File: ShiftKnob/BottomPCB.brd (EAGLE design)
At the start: 37.8 x 40.2 mm, 39 parts, among them IC2 7805DT, J1 AVR_SPI_PRG_6PTH, Q1 16MHz, Q2 MOSFET-NCHANNELSMD, Q3 MOSFET-PCHANNELSMD, Q4 MOSFET-NCHANNELSMD, Q5 MOSFET-NCHANNELSMD, Q6 MOSFET-NCHANNELSMD, U1 ATMEGA328

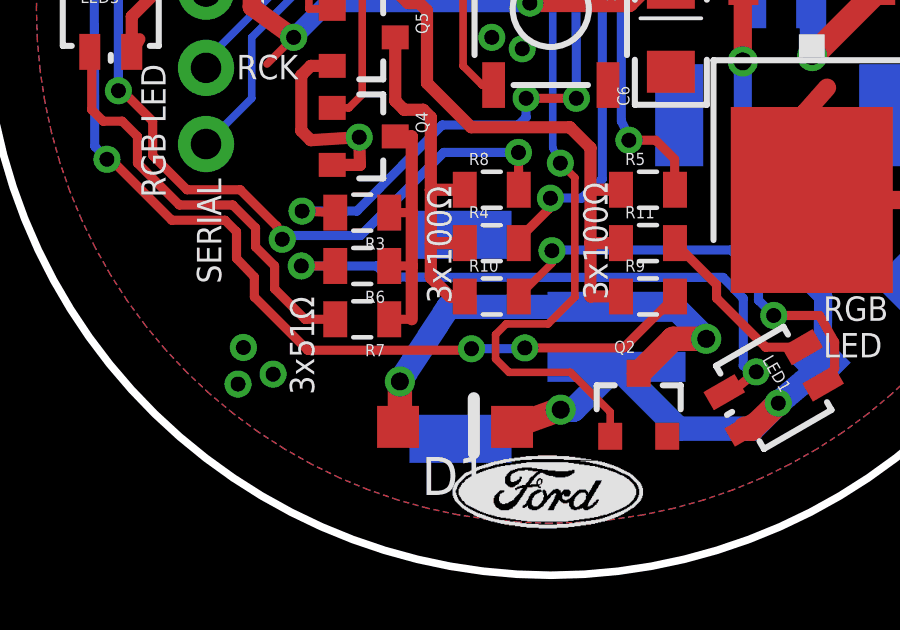
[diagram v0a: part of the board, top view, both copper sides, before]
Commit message: change red LED resistance from 50ohm to 100ohm.
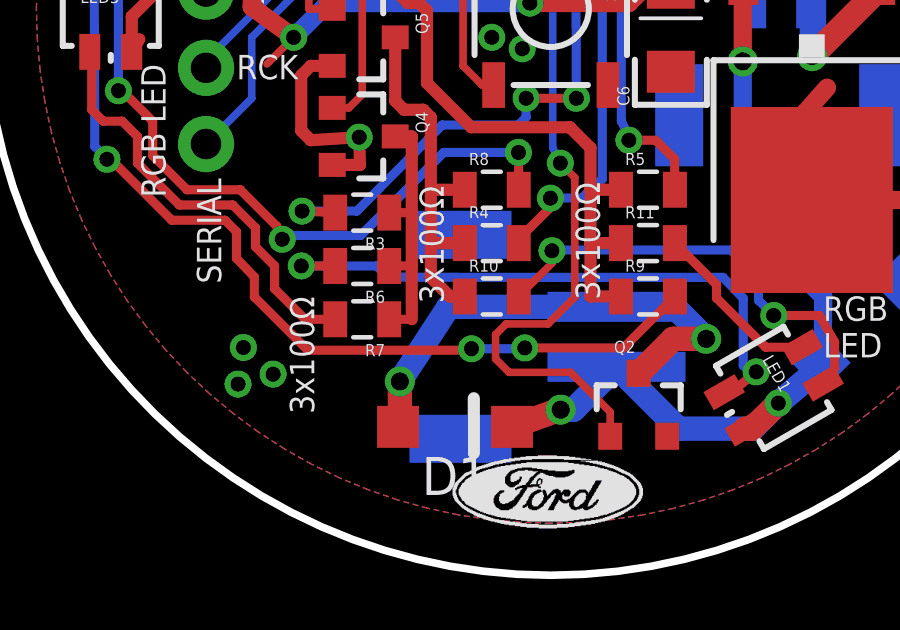
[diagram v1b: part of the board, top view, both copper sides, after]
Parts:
- R3, R6, R7: value 50 -> 100
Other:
- board text removed: "3x51Ω"
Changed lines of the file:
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@@
 <rectangle x1="15.7759" y1="22.3545" x2="16.4109" y2="22.3799" layer="22" rot="R90"/>
 <text x="20.386" y="24.577" size="0.8128" layer="21">BUT</text>
-<text x="12.893" y="12.004" size="0.8128" layer="21" rot="R270">3x51Ω</text>
-<text x="17.465" y="15.687" size="0.8128" layer="21" rot="R270">3x100Ω</text>
-<text x="22.672" y="15.814" size="0.8128" layer="21" rot="R270">3x100Ω</text>
+<text x="12.893" y="12.004" size="0.8128" layer="21" rot="R270">3x100Ω</text>
+<text x="17.211" y="15.687" size="0.8128" layer="21" rot="R270">3x100Ω</text>
+<text x="22.418" y="15.814" size="0.8128" layer="21" rot="R270">3x100Ω</text>
 <rectangle x1="21.1861" y1="4.2697" x2="21.7957" y2="4.2951" layer="21"/>
 <rectangle x1="20.7797" y1="4.2951" x2="22.1767" y2="4.3205" layer="21"/>
@@
 <element name="LED4" library="SparkFun" package="LED-0603" value="Red" x="29.403" y="26.863"/>
 <element name="R4" library="SparkFun-Resistors" package="0805" value="100" x="19.624" y="13.782"/>
-<element name="R3" library="SparkFun-Resistors" package="0805" value="50" x="15.306" y="14.798" rot="R180"/>
+<element name="R3" library="SparkFun-Resistors" package="0805" value="100" x="15.306" y="14.798" rot="R180"/>
 <element name="R5" library="SparkFun-Resistors" package="0805" value="100" x="24.831" y="15.56"/>
-<element name="R7" library="SparkFun-Resistors" package="0805" value="50" x="15.306" y="11.242" rot="R180"/>
+<element name="R7" library="SparkFun-Resistors" package="0805" value="100" x="15.306" y="11.242" rot="R180"/>
 <element name="R8" library="SparkFun-Resistors" package="0805" value="100" x="19.624" y="15.56"/>
 <element name="R9" library="SparkFun-Resistors" package="0805" value="100" x="24.831" y="12.004"/>
@@
 <element name="D1" library="diode" package="SOD123" value="MBR0520LT" x="18.3998" y="7.6556" rot="R180"/>
 <element name="LED1" library="SparkFun" package="LED-TRICOLOR-SMD" value="LED-TRICOLOR" x="29.022" y="8.956" rot="R300"/>
-<element name="R6" library="SparkFun-Resistors" package="0805" value="50" x="15.306" y="13.02" rot="R180"/>
+<element name="R6" library="SparkFun-Resistors" package="0805" value="100" x="15.306" y="13.02" rot="R180"/>
 <element name="R10" library="SparkFun-Resistors" package="0805" value="100" x="19.624" y="12.004"/>
 <element name="R11" library="SparkFun-Resistors" package="0805" value="100" x="24.831" y="13.782"/>

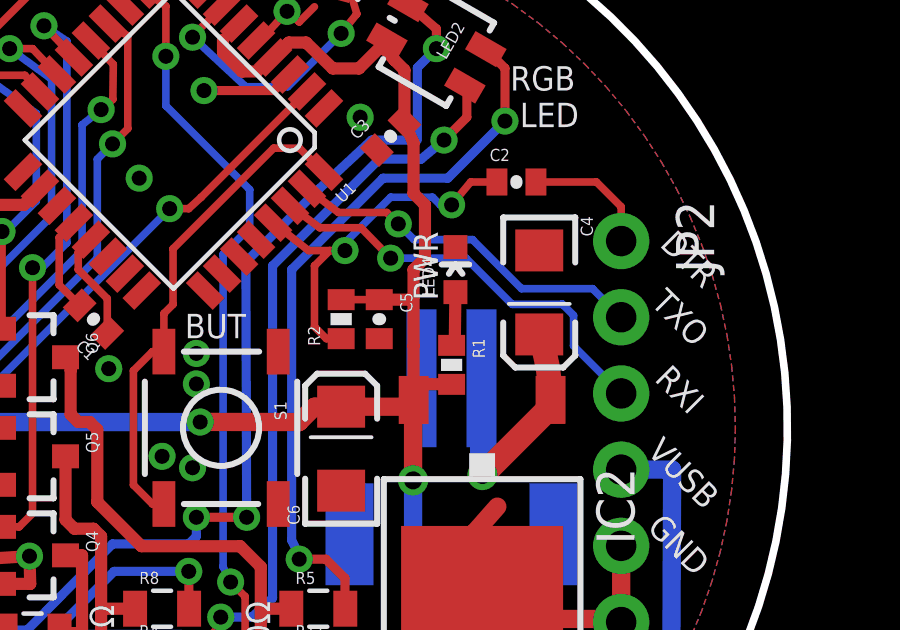
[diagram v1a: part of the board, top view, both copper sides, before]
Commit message: remove power LED and resistor. not needed as RGB leds turn on when 5V is applied during startup.
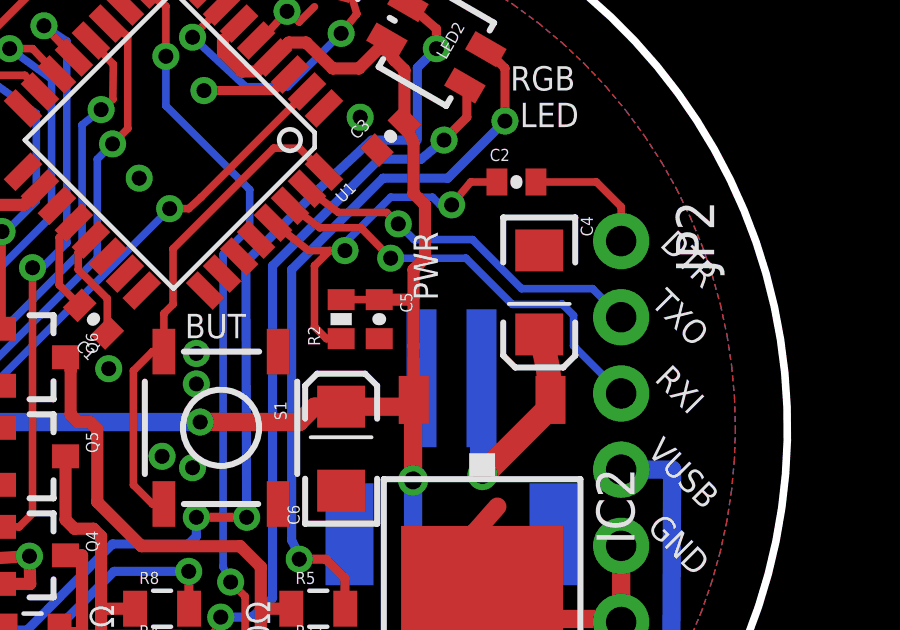
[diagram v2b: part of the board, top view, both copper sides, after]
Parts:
- removed LED4: Red, SparkFun:LED-0603
- removed R1: 10K, SparkFun:0402-RES
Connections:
- removed net N$3: LED4.A, R1.1
- net GND: no longer LED4.C
- net VCC: no longer R1.2
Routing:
- net N$3: track 1.91 -> 0.00 mm
- net VCC: track 94.5 -> 93.2 mm
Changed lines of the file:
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@@
 <element name="C5" library="SparkFun" package="0402-CAP" value="0.1uF" x="26.863" y="25.212" rot="R270"/>
 <element name="C6" library="SparkFun" package="EIA3216" value="10uF" x="25.593" y="20.894" rot="R90"/>
-<element name="R1" library="SparkFun" package="0402-RES" value="10K" x="29.276" y="23.688" rot="R270"/>
-<element name="LED4" library="SparkFun" package="LED-0603" value="Red" x="29.403" y="26.863"/>
 <element name="R4" library="SparkFun-Resistors" package="0805" value="100" x="19.624" y="13.782"/>
 <element name="R3" library="SparkFun-Resistors" package="0805" value="100" x="15.306" y="14.798" rot="R180"/>
@@
 <contactref element="C6" pad="C"/>
 <contactref element="C5" pad="2"/>
-<contactref element="LED4" pad="C"/>
 <contactref element="Q4" pad="2"/>
 <contactref element="Q5" pad="2"/>
@@
 <contactref element="C6" pad="A"/>
 <contactref element="C5" pad="1"/>
-<contactref element="R1" pad="2"/>
 <contactref element="LED2" pad="A"/>
 <contactref element="LED3" pad="A"/>
@@
 <wire x1="27.371" y1="33.848" x2="27.70361875" y2="33.51538125" width="0.4064" layer="1"/>
 <wire x1="27.70361875" y1="33.51538125" x2="27.70361875" y2="31.76761875" width="0.4064" layer="1"/>
-<wire x1="28.021" y1="23.053" x2="29.276" y2="23.038" width="0.4064" layer="1"/>
 <wire x1="25.593" y1="25.862" x2="26.863" y2="25.862" width="0.254" layer="1"/>
 <wire x1="26.863" y1="25.862" x2="27.894" y2="25.862" width="0.4064" layer="1"/>
@@
 <wire x1="26.863" y1="30.546" x2="23.307" y2="26.99" width="0.3048" layer="16"/>
 </signal>
-<signal name="N$3">
-<contactref element="R1" pad="1"/>
-<contactref element="LED4" pad="A"/>
-<wire x1="29.276" y1="24.338" x2="29.3792" y2="24.3126" width="0.4064" layer="1"/>
-<wire x1="29.3792" y1="24.3126" x2="29.403" y2="26.113" width="0.4064" layer="1"/>
-</signal>
 <signal name="N$4">

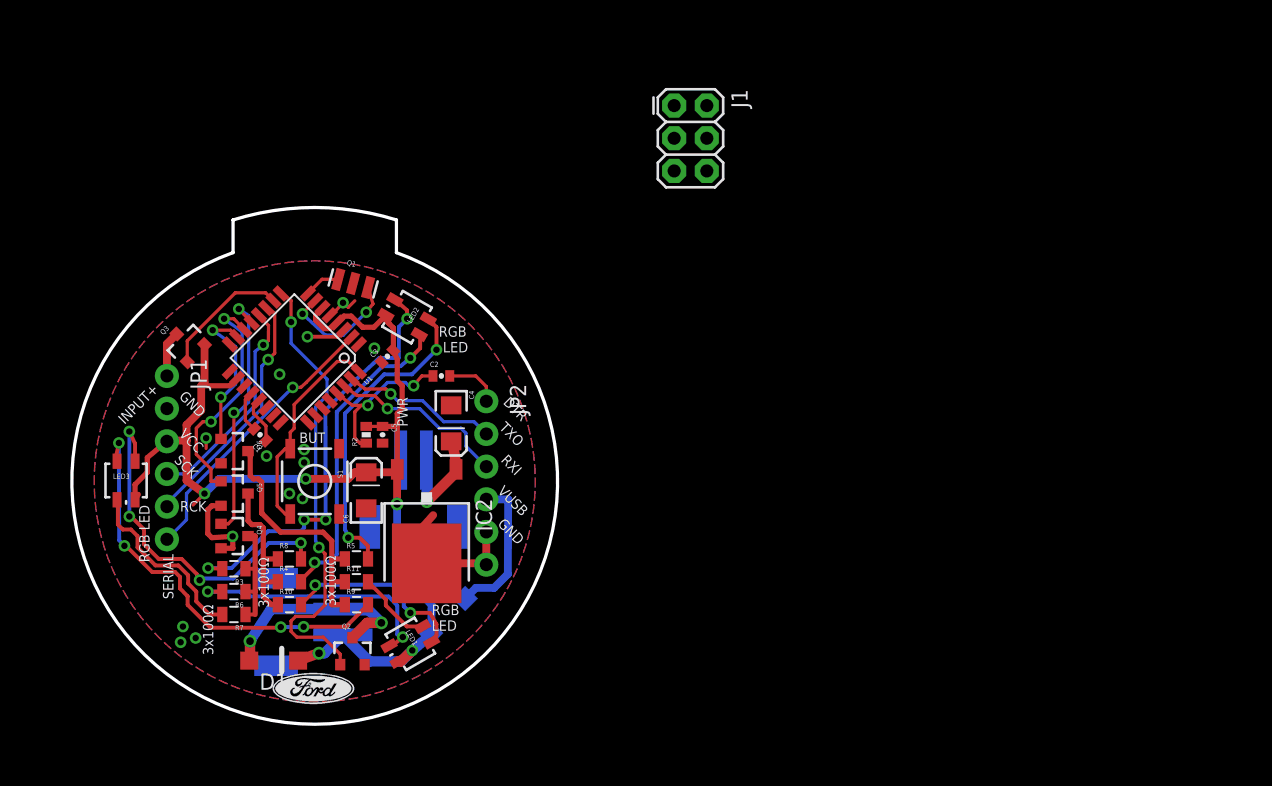
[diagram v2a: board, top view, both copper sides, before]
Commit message: finish the schematic for the FTDI chip. Need to rework the board layout still.
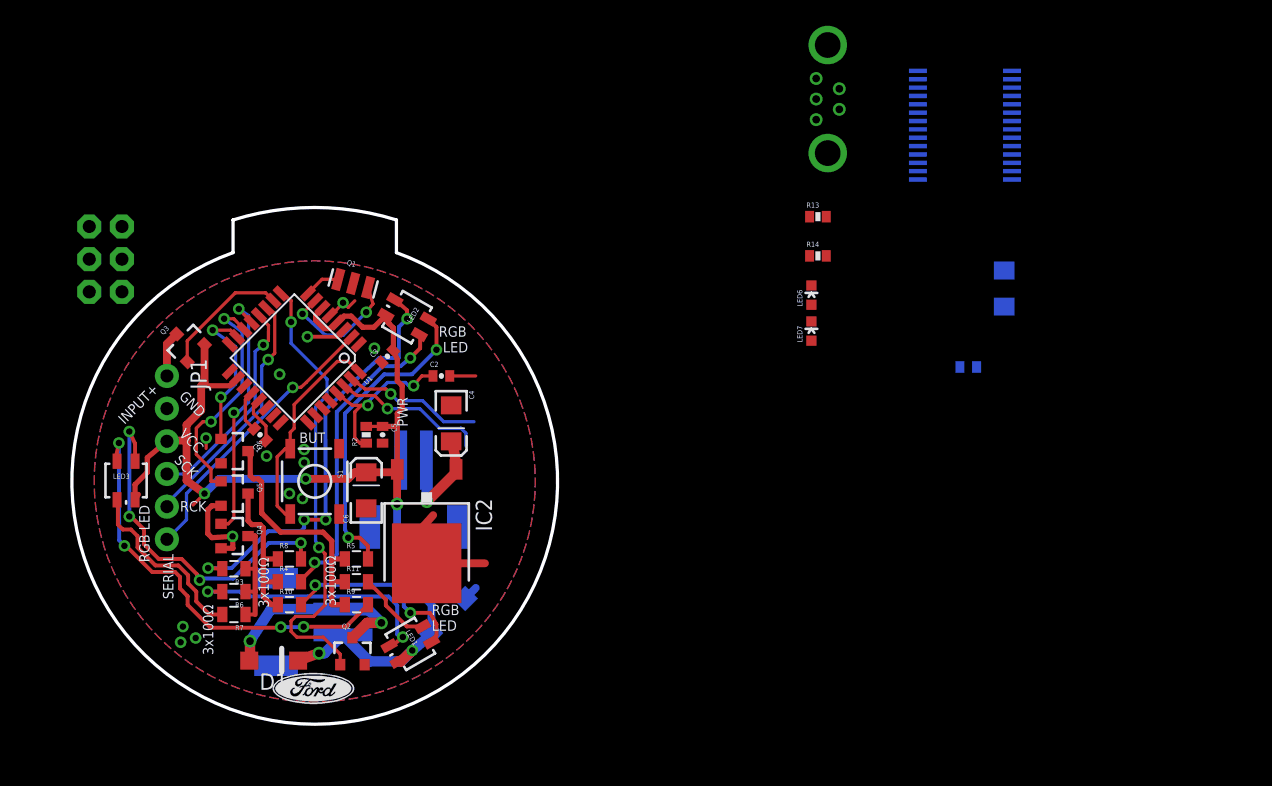
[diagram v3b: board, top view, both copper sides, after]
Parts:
- removed JP2: FTDI Basic, SparkFun-Connectors:1X06
- added C10: 10uF, SparkFun:EIA3216
- added C9: 0.1uF, SparkFun:0402-CAP
- added LED6: Red, SparkFun:LED-0603
- added LED7: Green, SparkFun:LED-0603
- added R13, R14: 1K, SparkFun:0402-RES
- added U$6: USB-MINI-B_VERTICAL, FORD_frames:USB-MINI-B_VERTICAL
- added U3: FT232RL-BASICSSOP, SparkFun-DigitalIC:SSOP28DB
- moved J1 43.9 mm to (6.60, 41.4), flipped to the bottom
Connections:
- new net 5V: R13.2, R14.2
- new net N$21: U$6.D+, U3.15
- new net N$22: U$6.D-, U3.16
- new net N$23: LED6.A, R13.1
- new net N$24: LED7.A, R14.1
- new net RXLED1: LED7.C, U3.22
- new net TXLED1: LED6.C, U3.23
- net DTR: now also U3.2; no longer JP2.1
- net GND: now also C10.C, C9.2, U$6.GND, U3.18, U3.21, U3.25, U3.26, U3.7; no longer JP2.5, JP2.6
- net RXI: now also U3.5; no longer JP2.3
- net TXO: now also U3.1; no longer JP2.2
- net VUSB: now also C10.A, C9.1, U$6.VUSB, U3.20, U3.4; no longer JP2.4
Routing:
- net VUSB: track 11.6 -> 1.17 mm
- net GND: track 28.5 -> 25.8 mm
- net DTR: track 4.33 -> 2.02 mm
- net RXI: track 14.2 -> 11.9 mm
- net TXO: track 12.2 -> 10.8 mm
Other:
- board text removed: "DTR"
- board text removed: "RXI"
- board text removed: "TXO"
- board text removed: "VUSB"

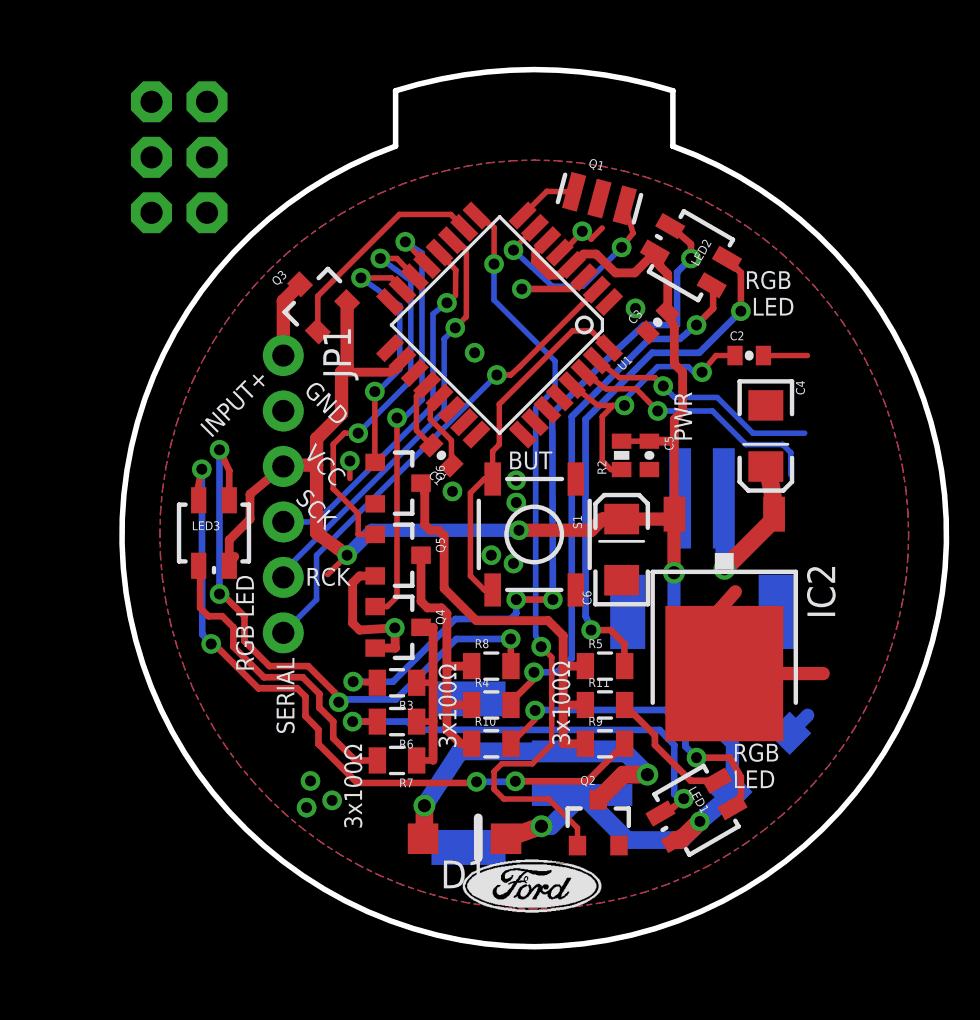
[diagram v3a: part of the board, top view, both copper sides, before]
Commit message: switch out RGB LEDs for Right-Angle RGBs from FORD_frames library. Still need to fix layout.
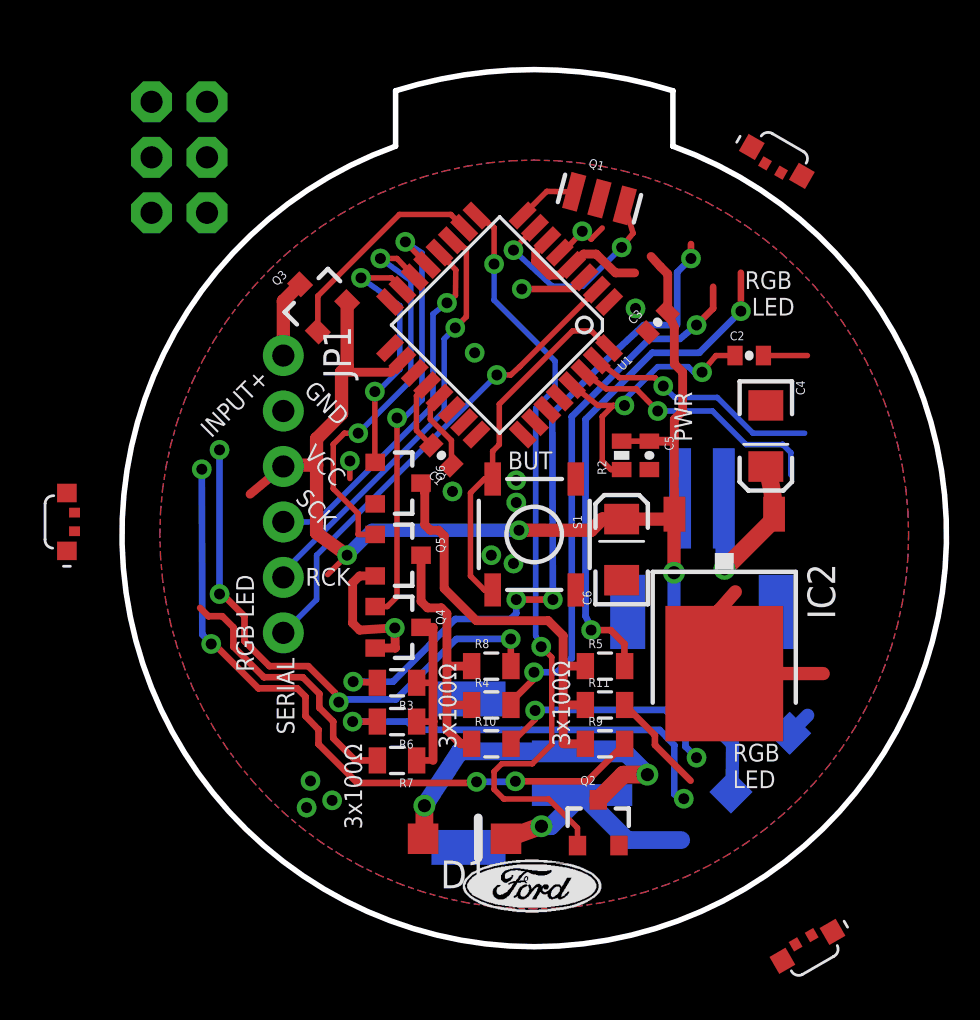
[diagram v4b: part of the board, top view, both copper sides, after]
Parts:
- LED1, LED2, LED3: value LED-TRICOLOR -> LED-RGB; device SparkFun:LED-TRICOLOR-SMD -> FORD_frames:LED-RGB_SMD-RIGHTANGLE
- moved LED1 8.04 mm to (34.1, 2.73), turned to 210 degrees
- moved LED3 6.76 mm to (0.19, 22.2), turned to 90 degrees
- moved LED2 5.84 mm to (32.7, 38.7), turned to 330 degrees
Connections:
- net N$10: now also LED1.4; no longer LED1.G
- net N$16: now also LED3.1; no longer LED3.B
- net N$25: now also LED2.1; no longer LED2.B
- net N$4: now also LED2.3; no longer LED2.R
- net N$5: now also LED2.4; no longer LED2.G
- net N$6: now also LED3.3; no longer LED3.R
- net N$7: now also LED1.1; no longer LED1.B
- net N$8: now also LED3.4; no longer LED3.G
- net N$9: now also LED1.3; no longer LED1.R
- net VCC: now also LED1.2, LED2.2, LED3.2; no longer LED1.A, LED2.A, LED3.A
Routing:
- net VCC: track 93.2 -> 82.9 mm, vias 5 -> 4
- net N$7: track 14.8 -> 10.7 mm
- net N$16: track 27.6 -> 25.2 mm
- net N$6: track 14.3 -> 12.3 mm
- net N$8: track 32.8 -> 31.4 mm
- net N$9: track 20.4 -> 19.0 mm
- net N$4: track 33.3 -> 32.0 mm
- net N$10: track 5.94 -> 4.72 mm
- net N$5: track 24.3 -> 23.4 mm
